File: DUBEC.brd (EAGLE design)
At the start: 40 x 21.4 mm, 72 parts

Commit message: Tweaks
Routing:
- net GND: track 34.1 -> 35.7 mm
- net 5V: track 44.4 -> 43.5 mm
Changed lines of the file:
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@@
 <grid distance="0.125" unitdist="mm" unit="mm" style="lines" multiple="8" display="yes" altdistance="0.0625" altunitdist="mm" altunit="mm"/>
 <layers>
-<layer number="1" name="Top" color="2" fill="1" visible="yes" active="yes"/>
+<layer number="1" name="Top" color="2" fill="1" visible="no" active="yes"/>
 <layer number="2" name="Route2" color="9" fill="1" visible="no" active="yes"/>
 <layer number="3" name="Route3" color="4" fill="3" visible="no" active="no"/>
 <layer number="14" name="Route14" color="1" fill="6" visible="no" active="no"/>
-<layer number="15" name="Route15" color="14" fill="1" visible="yes" active="yes"/>
+<layer number="15" name="Route15" color="14" fill="1" visible="no" active="yes"/>
 <layer number="16" name="Bottom" color="5" fill="1" visible="yes" active="yes"/>
 <layer number="17" name="Pads" color="10" fill="1" visible="yes" active="yes"/>
@@
 <layer number="20" name="Dimension" color="15" fill="1" visible="yes" active="yes"/>
 <layer number="21" name="tPlace" color="15" fill="1" visible="no" active="yes"/>
-<layer number="22" name="bPlace" color="7" fill="1" visible="no" active="yes"/>
-<layer number="23" name="tOrigins" color="15" fill="1" visible="yes" active="yes"/>
+<layer number="22" name="bPlace" color="7" fill="1" visible="yes" active="yes"/>
+<layer number="23" name="tOrigins" color="15" fill="1" visible="no" active="yes"/>
 <layer number="24" name="bOrigins" color="15" fill="1" visible="yes" active="yes"/>
 <layer number="25" name="tNames" color="7" fill="1" visible="no" active="yes"/>
@@
 <layer number="27" name="tValues" color="7" fill="1" visible="no" active="yes"/>
 <layer number="28" name="bValues" color="7" fill="1" visible="no" active="yes"/>
-<layer number="29" name="tStop" color="4" fill="1" visible="yes" active="yes"/>
+<layer number="29" name="tStop" color="4" fill="1" visible="no" active="yes"/>
 <layer number="30" name="bStop" color="7" fill="6" visible="yes" active="yes"/>
-<layer number="31" name="tCream" color="7" fill="4" visible="yes" active="yes"/>
+<layer number="31" name="tCream" color="7" fill="4" visible="no" active="yes"/>
 <layer number="32" name="bCream" color="7" fill="5" visible="yes" active="yes"/>
-<layer number="33" name="tFinish" color="6" fill="3" visible="yes" active="yes"/>
+<layer number="33" name="tFinish" color="6" fill="3" visible="no" active="yes"/>
 <layer number="34" name="bFinish" color="6" fill="6" visible="yes" active="yes"/>
-<layer number="35" name="tGlue" color="7" fill="4" visible="yes" active="yes"/>
+<layer number="35" name="tGlue" color="7" fill="4" visible="no" active="yes"/>
 <layer number="36" name="bGlue" color="7" fill="5" visible="yes" active="yes"/>
-<layer number="37" name="tTest" color="7" fill="1" visible="yes" active="yes"/>
+<layer number="37" name="tTest" color="7" fill="1" visible="no" active="yes"/>
 <layer number="38" name="bTest" color="7" fill="1" visible="yes" active="yes"/>
-<layer number="39" name="tKeepout" color="4" fill="11" visible="yes" active="yes"/>
+<layer number="39" name="tKeepout" color="4" fill="11" visible="no" active="yes"/>
 <layer number="40" name="bKeepout" color="1" fill="11" visible="yes" active="yes"/>
-<layer number="41" name="tRestrict" color="14" fill="10" visible="yes" active="yes"/>
+<layer number="41" name="tRestrict" color="14" fill="10" visible="no" active="yes"/>
 <layer number="42" name="bRestrict" color="1" fill="10" visible="yes" active="yes"/>
 <layer number="43" name="vRestrict" color="2" fill="10" visible="no" active="yes"/>
 <layer number="44" name="Drills" color="7" fill="1" visible="no" active="yes"/>
-<layer number="45" name="Holes" color="7" fill="1" visible="no" active="yes"/>
+<layer number="45" name="Holes" color="7" fill="1" visible="yes" active="yes"/>
 <layer number="46" name="Milling" color="3" fill="1" visible="no" active="yes"/>
 <layer number="47" name="Measures" color="7" fill="1" visible="yes" active="yes"/>
-<layer number="48" name="Document" color="7" fill="1" visible="no" active="yes"/>
+<layer number="48" name="Document" color="7" fill="1" visible="yes" active="yes"/>
 <layer number="49" name="Reference" color="7" fill="1" visible="no" active="yes"/>
 <layer number="50" name="dxf" color="7" fill="1" visible="no" active="no"/>
 <layer number="51" name="tDocu" color="7" fill="1" visible="no" active="yes"/>
-<layer number="52" name="bDocu" color="7" fill="1" visible="no" active="yes"/>
+<layer number="52" name="bDocu" color="7" fill="1" visible="yes" active="yes"/>
 <layer number="53" name="tGND_GNDA" color="7" fill="9" visible="no" active="no"/>
 <layer number="54" name="bGND_GNDA" color="1" fill="9" visible="no" active="no"/>
@@
 <layer number="100" name="Muster" color="7" fill="1" visible="no" active="no"/>
 <layer number="101" name="Patch_Top" color="12" fill="4" visible="no" active="yes"/>
-<layer number="102" name="tPolarity" color="7" fill="1" visible="yes" active="yes"/>
+<layer number="102" name="tPolarity" color="7" fill="1" visible="no" active="yes"/>
 <layer number="103" name="tMap" color="7" fill="1" visible="no" active="yes"/>
 <layer number="104" name="Name" color="16" fill="1" visible="no" active="yes"/>
-<layer number="105" name="tPlate" color="7" fill="1" visible="yes" active="yes"/>
+<layer number="105" name="tPlate" color="7" fill="1" visible="no" active="yes"/>
 <layer number="106" name="bPlate" color="7" fill="1" visible="no" active="yes"/>
-<layer number="107" name="tLabels" color="15" fill="1" visible="yes" active="yes"/>
+<layer number="107" name="tLabels" color="15" fill="1" visible="no" active="yes"/>
 <layer number="108" name="tplace-old" color="10" fill="1" visible="no" active="yes"/>
 <layer number="109" name="ref-old" color="11" fill="1" visible="no" active="yes"/>
@@
 <wire x1="36.5" y1="1" x2="36.75" y2="0.75" width="0.254" layer="1"/>
 <wire x1="36.75" y1="0.75" x2="38.75" y2="0.75" width="0.254" layer="1"/>
+<wire x1="37.875" y1="13.125" x2="39" y2="14.25" width="0.635" layer="16"/>
 </signal>
 <signal name="12V">
@@
 <wire x1="15.75" y1="16.75" x2="15.75" y2="17.5" width="0.4" layer="1"/>
 <via x="29.625" y="14.5" extent="1-16" drill="0.5"/>
-<wire x1="29.625" y1="14.5" x2="29.625" y2="16.375" width="1.016" layer="15"/>
+<wire x1="29.625" y1="14.5" x2="29.625" y2="16.125" width="1.016" layer="15"/>
+<wire x1="29.625" y1="16.125" x2="29.625" y2="16.375" width="1.016" layer="15"/>
 <wire x1="29.625" y1="16.375" x2="29.625" y2="18.25" width="1.016" layer="15"/>
 <via x="29.625" y="16.375" extent="1-16" drill="0.5"/>
@@
 <via x="17.25" y="13" extent="1-16" drill="0.3"/>
 <wire x1="17.25" y1="13" x2="17.25" y2="14.875" width="0.3302" layer="15"/>
-<wire x1="29.625" y1="18.25" x2="35.75" y2="18.25" width="1" layer="15"/>
-<wire x1="35.75" y1="18.25" x2="37.875" y2="16.125" width="1" layer="15"/>
 <wire x1="16.625" y1="12.875" x2="16.75" y2="13" width="0.4" layer="1"/>
 <wire x1="16.75" y1="13" x2="17.25" y2="13" width="0.4" layer="1"/>
 <contactref element="5COUT2" pad="1"/>
 <contactref element="5COUT1" pad="A"/>
+<wire x1="37.875" y1="16.125" x2="29.625" y2="16.125" width="1.016" layer="15"/>
 </signal>
 <signal name="12V_FB">
@@
 <wire x1="14" y1="16.125" x2="14.625" y2="16.125" width="0.4" layer="1"/>
 <wire x1="2" y1="10.125" x2="4.5" y2="10.125" width="0.3302" layer="15"/>
-<wire x1="4.5" y1="10.125" x2="8.875" y2="14.5" width="0.3302" layer="15"/>
-<wire x1="8.875" y1="14.5" x2="13" y2="14.5" width="0.3302" layer="15"/>
-<wire x1="13" y1="14.5" x2="14.625" y2="16.125" width="0.3302" layer="15"/>
+<wire x1="4.5" y1="10.125" x2="8.5" y2="14.125" width="0.3302" layer="15"/>
+<wire x1="8.5" y1="14.125" x2="12.625" y2="14.125" width="0.3302" layer="15"/>
+<wire x1="12.625" y1="14.125" x2="14.625" y2="16.125" width="0.3302" layer="15"/>
 </signal>
 <signal name="GATE_MAIN_B" class="2">

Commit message: Tweaks
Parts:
- moved R3 2.58 mm to (6.12, 16.4), turned to 180 degrees
- moved RRSPU 2.08 mm to (8.25, 18.6), turned to 270 degrees
- moved AVRISP 0.18 mm to (4.12, 20.0)
- moved D3 0.18 mm to (5.88, 11.8)
- moved DAUXR 0.18 mm to (6.12, 15.2)
- moved RA2 0.18 mm to (6.12, 14.1)
- moved RA3 0.18 mm to (6.12, 13.0)
- moved CMCU 0.12 mm to (8.25, 16.8)
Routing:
- net RESET: track 11.1 -> 14.0 mm
- net LED_RED: track 3.74 -> 2.19 mm
- net 5V_MCU: track 15.7 -> 14.5 mm
- net SCK: track 15.4 -> 14.6 mm
- net MOSI: track 14.0 -> 13.5 mm

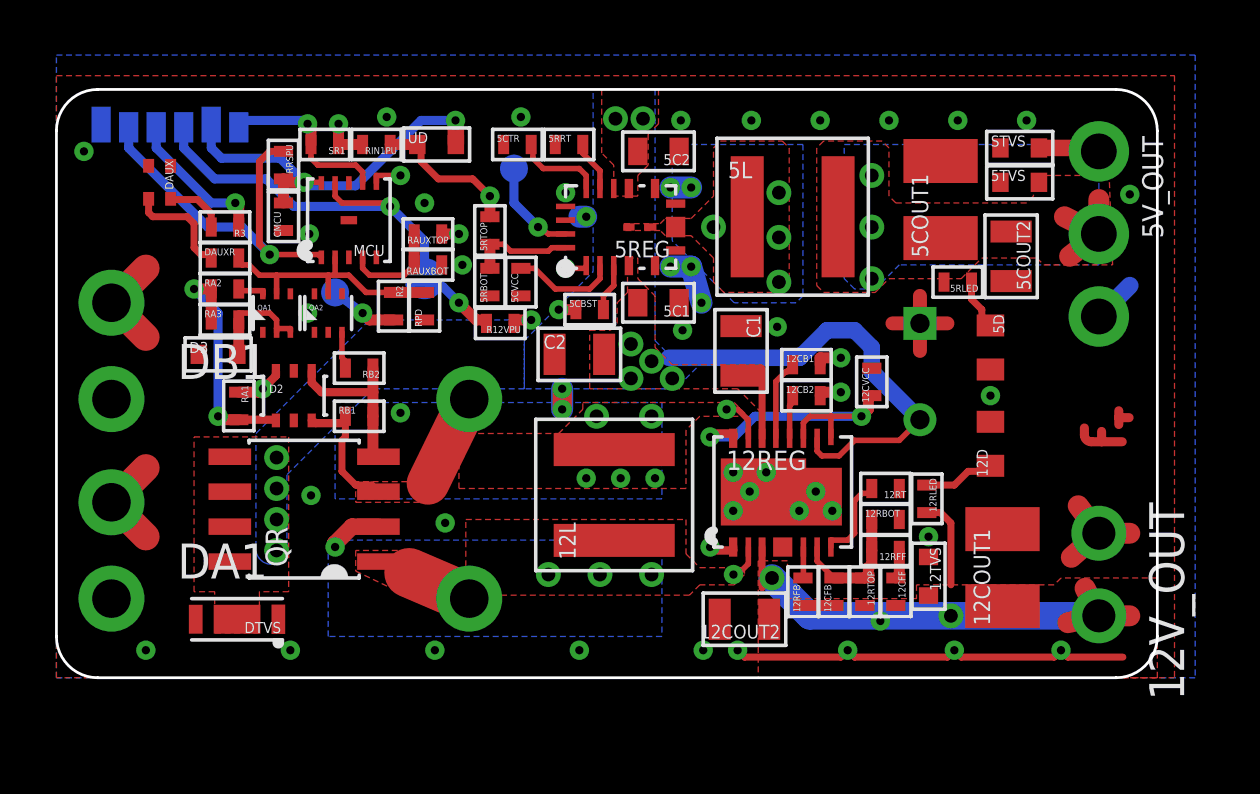
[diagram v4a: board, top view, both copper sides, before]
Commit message: Board fixes and isolation
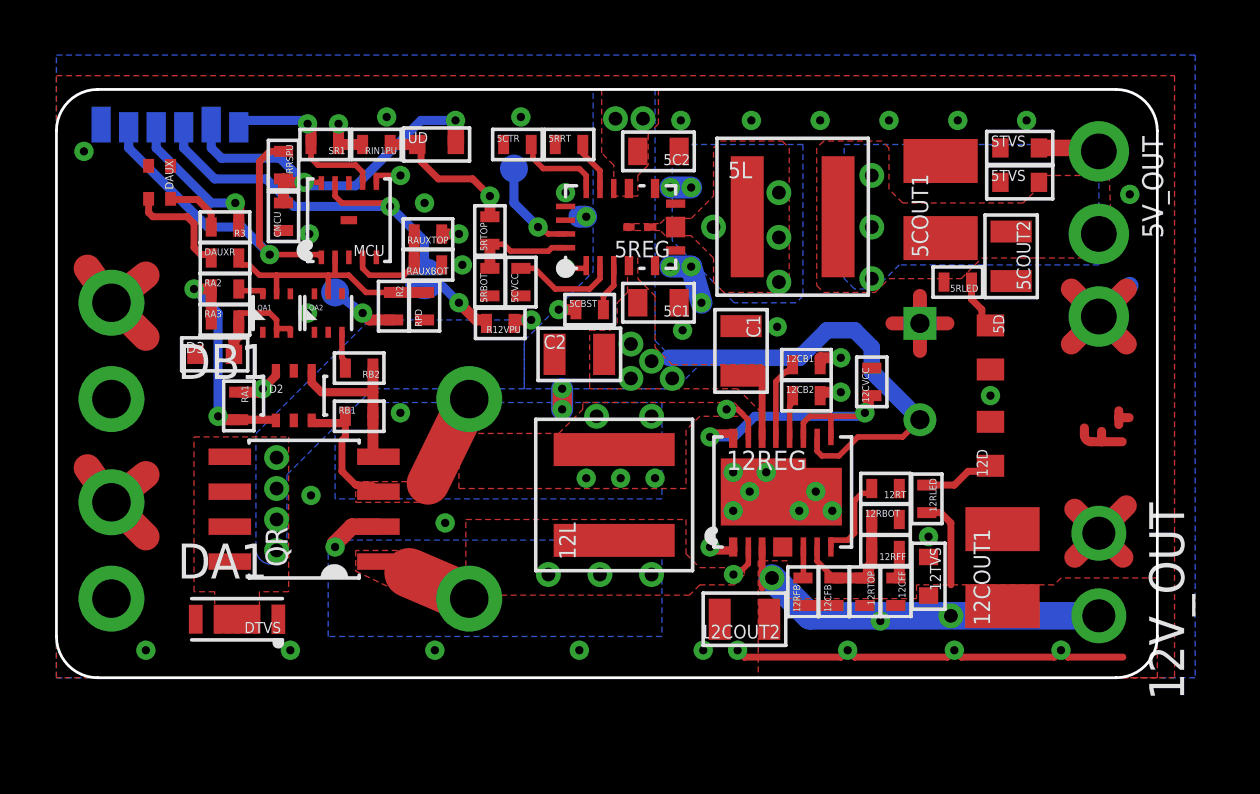
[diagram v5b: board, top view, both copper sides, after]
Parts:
- moved D3 0.12 mm to (5.75, 11.8)
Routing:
- net GND: track 35.7 -> 45.5 mm
- net 5V: track 43.5 -> 39.5 mm
- net 12V: track 33.6 -> 30.2 mm

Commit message: Bored wanking
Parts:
- C1, C2: value 22uF -> (none)
- moved RIN1PU 0.38 mm to (12.0, 19.4)
- moved SR1 0.38 mm to (10.1, 19.4)
- moved UD 0.38 mm to (14.2, 19.4)
- moved R2 0.25 mm to (12.2, 13.2)
- moved RAUXBOT 0.25 mm to (13.5, 14.8)
- moved RAUXTOP 0.25 mm to (13.5, 15.9)
- moved RPD 0.25 mm to (13.4, 13.2)
- moved SJ1 0.12 mm to (13.2, 14.5)
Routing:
- net GND: track 45.5 -> 31.2 mm, vias 46 -> 52
- net 35V: track 38.9 -> 48.2 mm, vias 10 -> 15
- net 5V: track 39.5 -> 43.5 mm
- net 12V: track 30.2 -> 32.7 mm
- net 12V_SW1: track 9.70 -> 8.32 mm

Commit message: Tweaks
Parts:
- moved 5V_PG 0.38 mm to (16.6, 18.9)
- moved 12CVCC 0.28 mm to (29.4, 10.6)
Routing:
- net 5V: track 43.5 -> 44.6 mm
- net 12VCC: track 11.5 -> 11.0 mm

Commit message: Kelvinize
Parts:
- moved CSNUB 0.50 mm to (31.9, 11.1), turned to 270 degrees
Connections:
- new net AGND: 12CVCC.2, 12RBOT.2, 12RT.1, 5CVCC.1, 5RBOT.1, CMCU.1, MCU.11, MCU.5, RAUXBOT.1
- net GND: no longer 12CVCC.2, 12RBOT.2, 12RT.1, 5CVCC.1, 5RBOT.1, CMCU.1, MCU.11, MCU.5, RAUXBOT.1
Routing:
- net AGND: track 0.00 -> 20.7 mm, vias 0 -> 2
- net 35V: track 48.1 -> 49.1 mm, vias 15 -> 16
- net GND: vias 52 -> 49
- added copper zone on layer 1, net AGND
